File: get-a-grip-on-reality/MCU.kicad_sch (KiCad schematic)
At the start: 22 parts, among them J12 Battery Connector MCU, J13 Conn_01x05_Pin, P1 USB_C_Plug_USB2.0, U1 TLV76733DRVx, U2 ESP32-S3-WROOM-1, U3 D3V3XA4B10LP

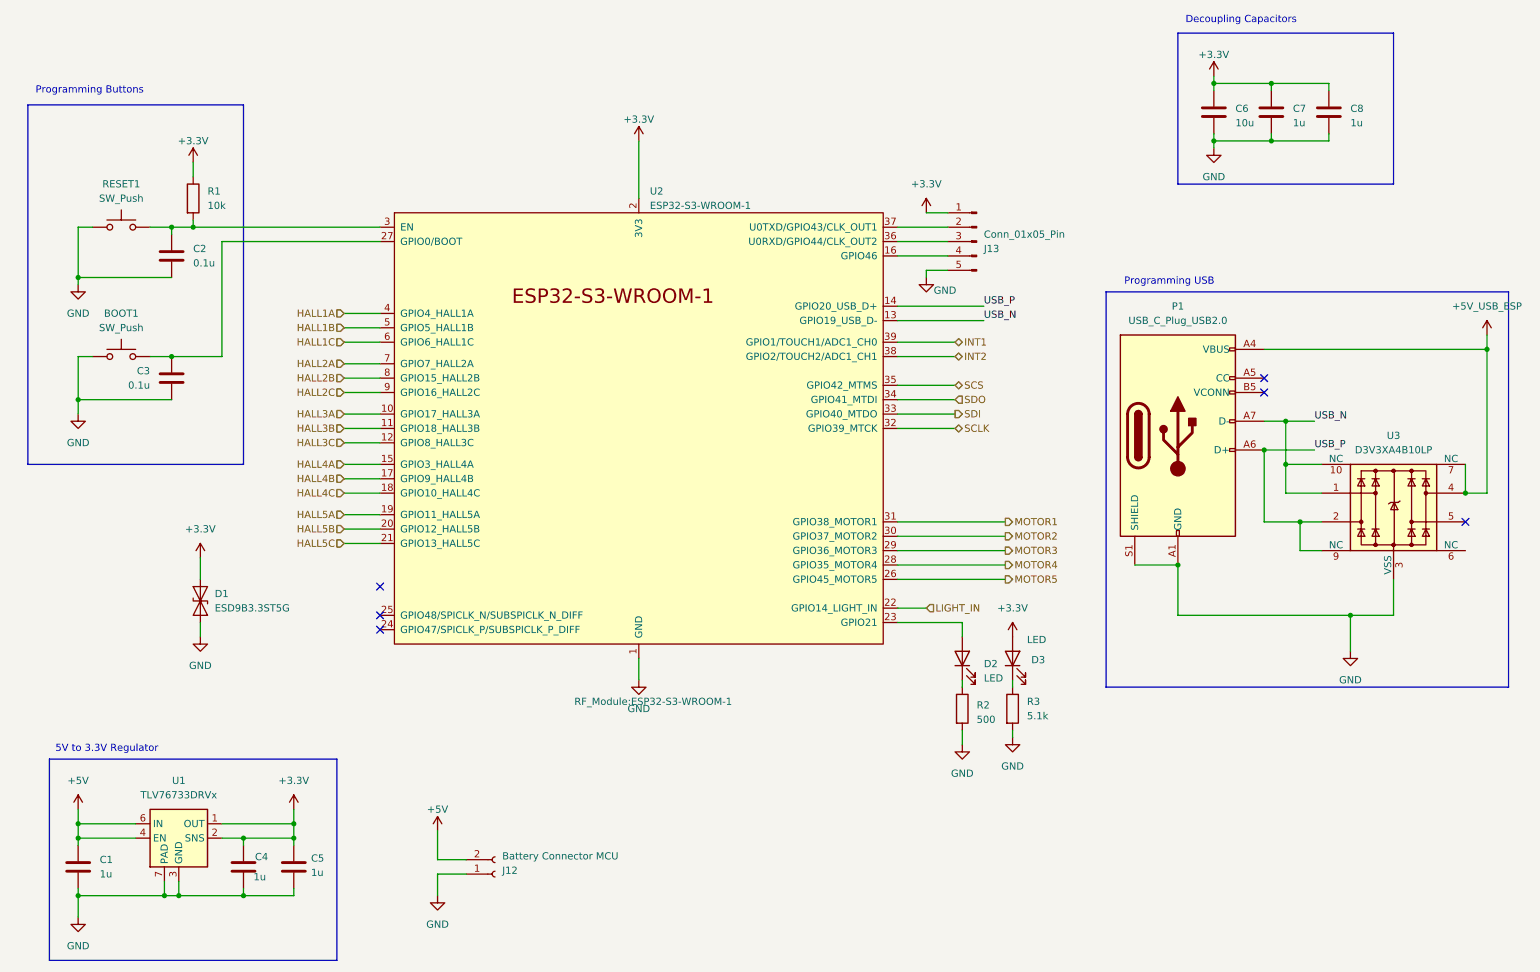
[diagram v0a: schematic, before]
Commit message: add mobile demo and rtos version of glove, improve schematic
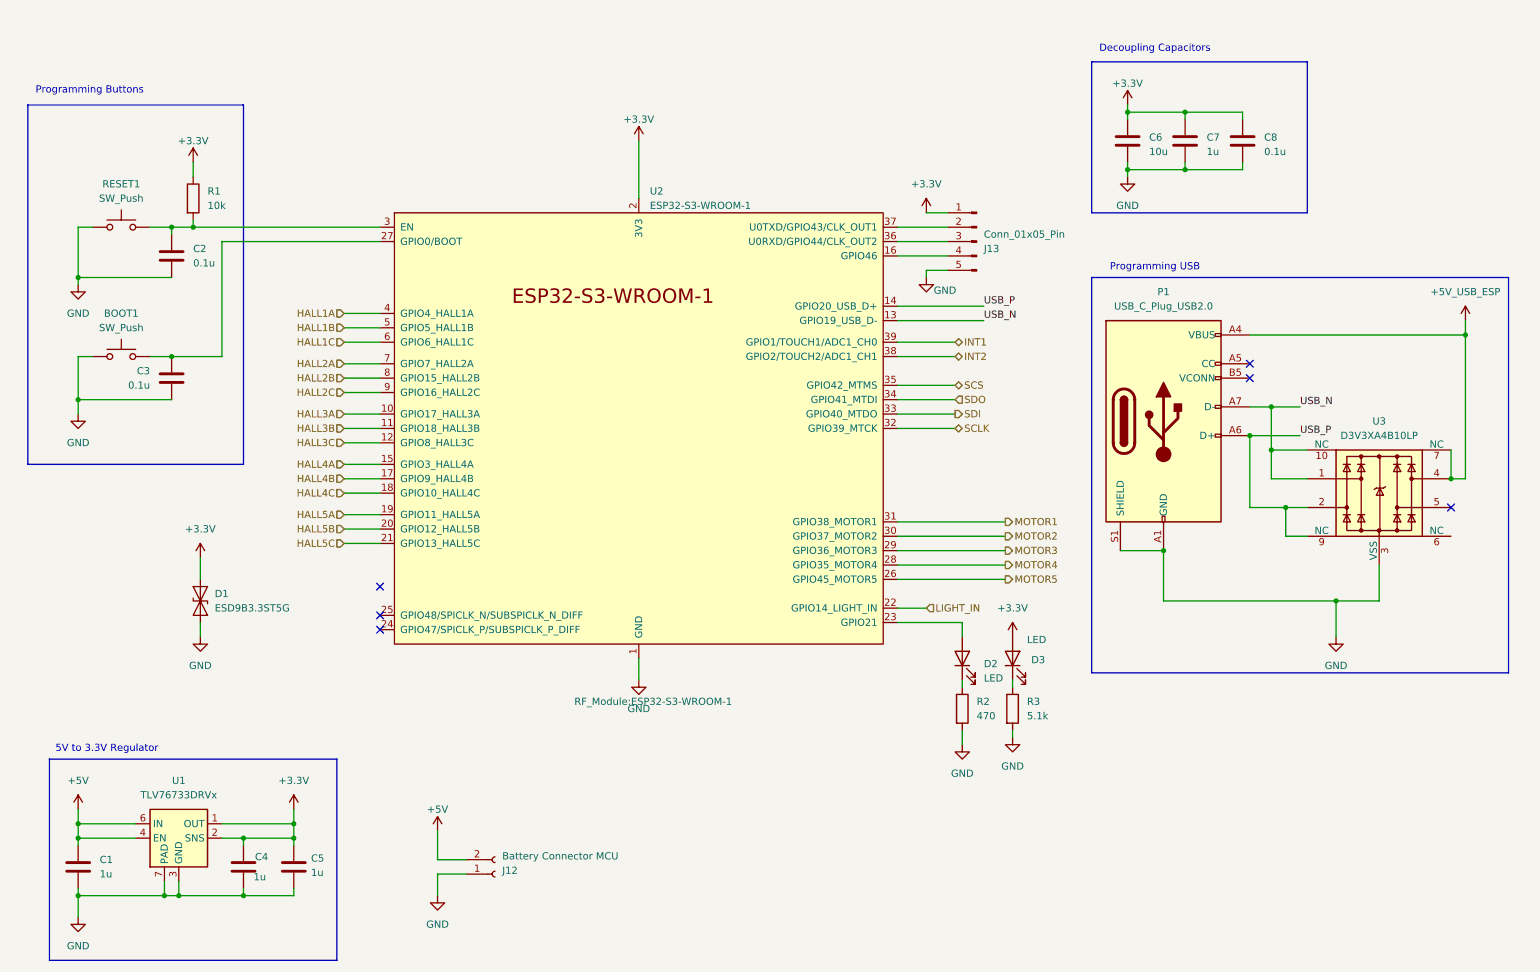
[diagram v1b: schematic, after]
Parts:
- C8: value 1u -> 0.1u
- R2: value 500 -> 470
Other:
- moved on the sheet: C6, C7, C8, P1, U3

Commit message: change to have working rtos code
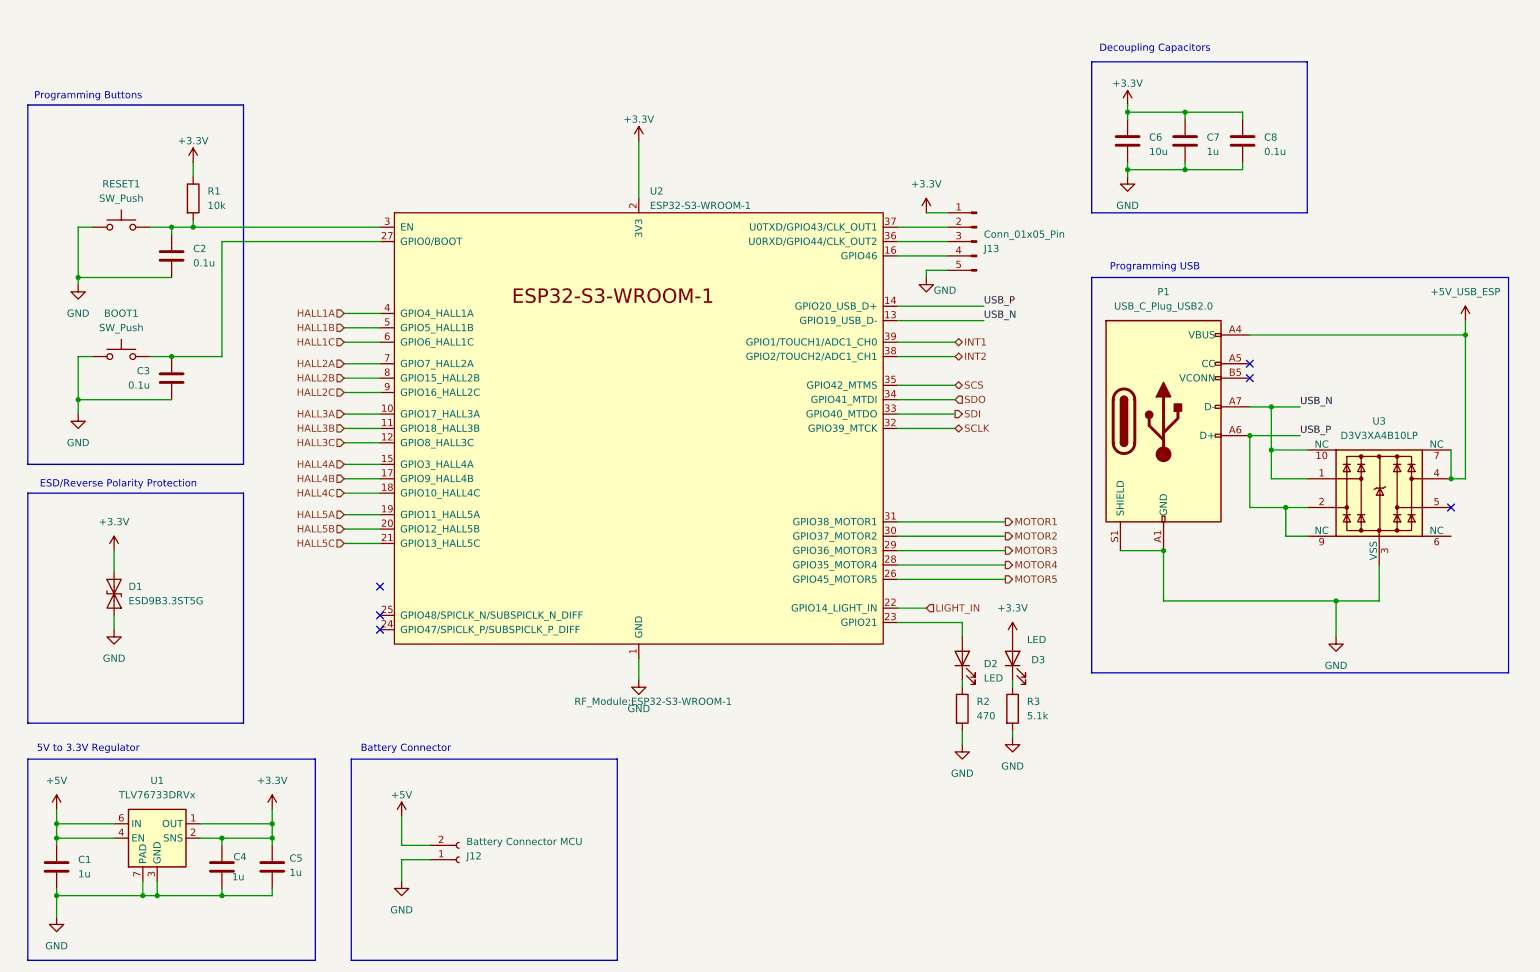
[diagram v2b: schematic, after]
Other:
- note added: "Battery Connector"
- note added: "ESD/Reverse Polarity Protection"
- moved on the sheet: C1, C4, C5, D1, J12, U1
